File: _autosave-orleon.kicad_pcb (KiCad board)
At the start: 6 copper layers, 32 x 32 mm, 83 parts, among them J103 Conn_ARM_JTAG_SWD_10, Q1 SBC847, SW101 CK_KMS2xxG, SW102 CK_KMS2xxG, U10 LIS2DH, U101 NRF52840-CKAA-F-R, U102 WLA.04, U103 ATECC608B-MAHDA, U104 LF21115TMR, U105 BME280, U106 MP34DT05TR-A, Y101 32MHz, Y102 32.768K

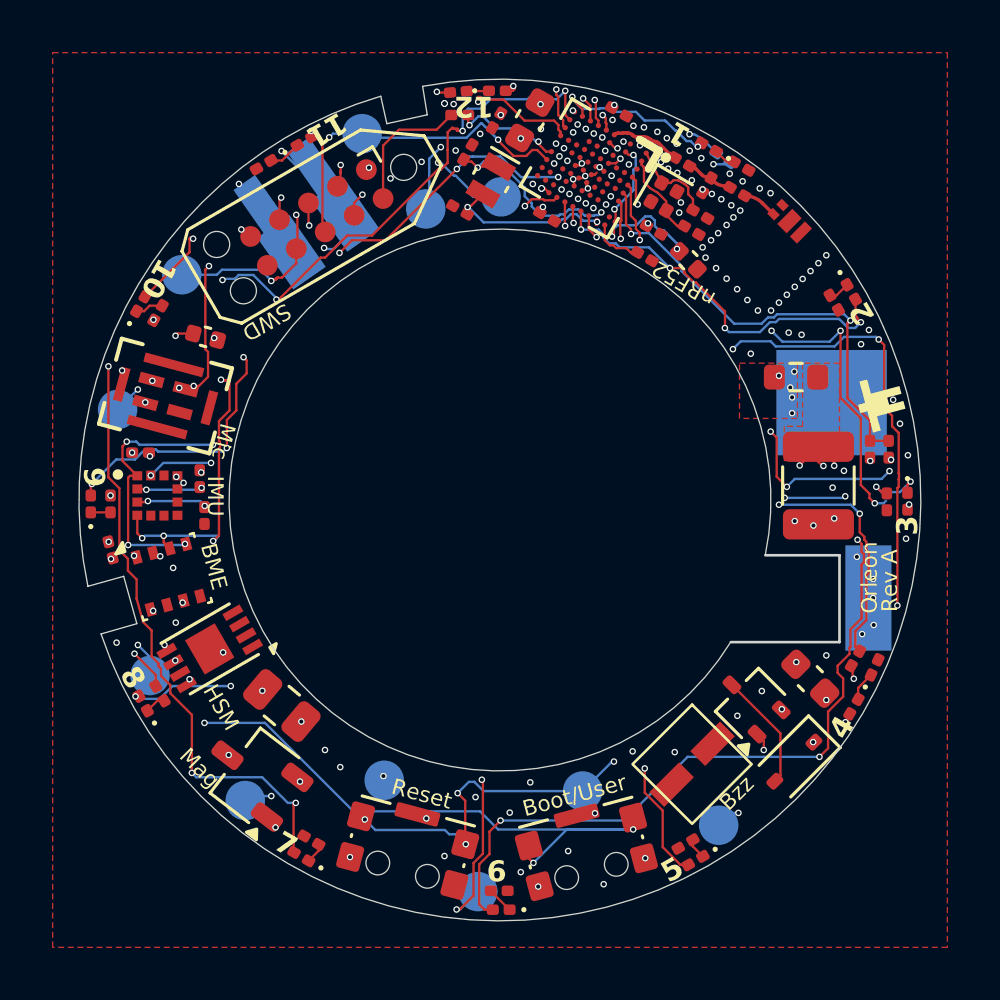
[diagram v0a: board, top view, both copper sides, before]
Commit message: Board files orleon-a-202502281452.zip (rev A candidate) bounced back from JLC. Started moving vias and widening BGA pads for their process.
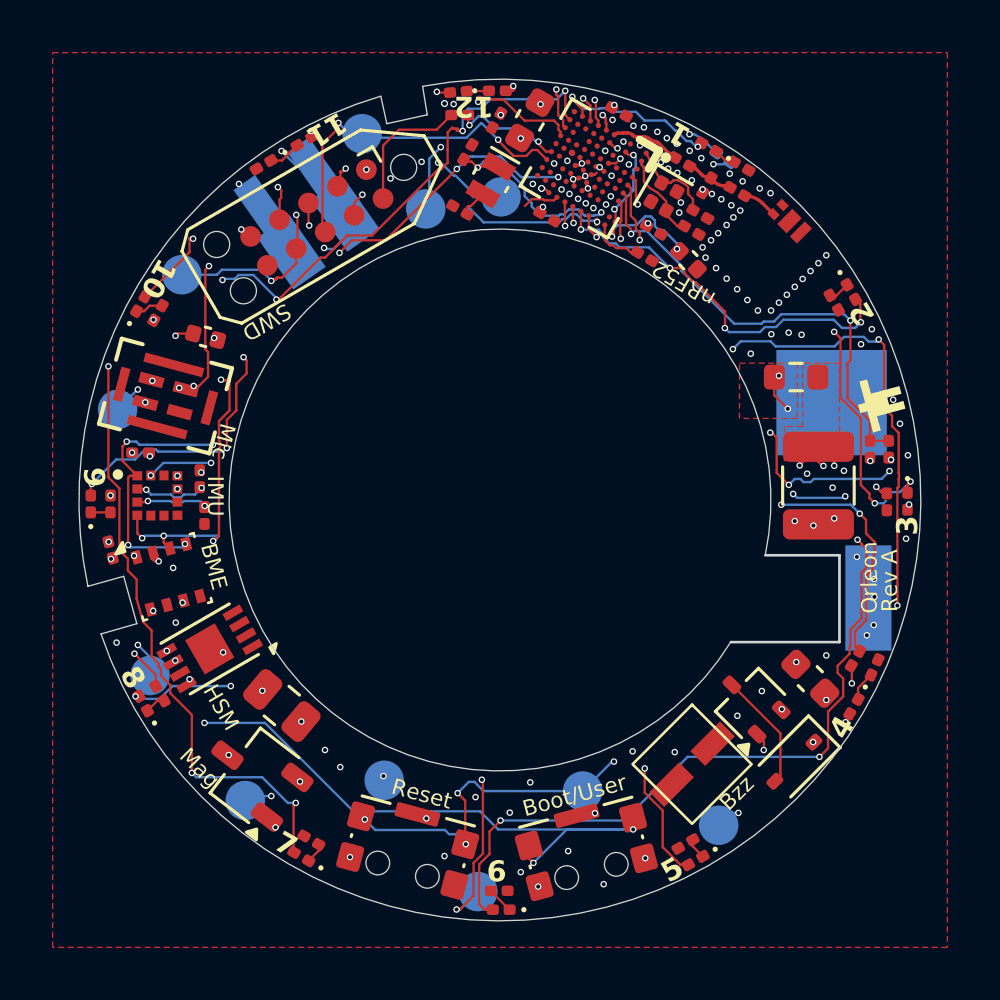
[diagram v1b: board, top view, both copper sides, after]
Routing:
- net /0.12/T1: track 36.0 -> 37.9 mm, vias 2 -> 1
- net /CR2032_IN: track 0.00 -> 1.61 mm, vias 5 -> 2
- net GND: track 27.3 -> 25.8 mm, vias 120 -> 117
- net /SWCLK: track 17.2 -> 17.6 mm, vias 3 -> 2
- net /LED05: track 39.9 -> 40.1 mm, vias 2 -> 1
- net /SWDIO: track 14.0 -> 13.9 mm, vias 3 -> 2
- net VCC: track 7.01 -> 6.89 mm, vias 32 -> 30
- net /1.00/T0: track 35.6 -> 35.5 mm, vias 2 -> 1
- net Net-(U101B-DEC5): vias 2 -> 1
- net Net-(U101A-P0.01/XL2): vias 2 -> 1
- net /MIC_CLK: vias 4 -> 3
- net /LED10: vias 2 -> 1
